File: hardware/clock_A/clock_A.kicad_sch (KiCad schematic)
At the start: 225 parts, among them J1 RJ45, J12 Conn_01x08_Pin, J14 Conn_01x02_Pin, J2 Conn_01x03, J4 USB_C_Receptacle, J5 Conn_01x06_Pin, J6 Conn_01x03_Pin, J8 Conn_01x02_Pin, Q1 2N7002, Q10 2N7002, Q9 2N7002, SW1 SW_Push_4PDT, SW2 SW_SPDT, U1 ADA4807-1, U10 STM32F405RGTx, U11 AMS1117-3.3, U12 BA50DD0WHFP-TR, U13 M24C02-RMN, U14 CH340C, U15 USBLC6-2P6, U16 TLV3603DCKR, U17 SN74LVC1G14DBV, U18 TMP112AIDRLR, U19 SN74LVC1G14DBV, U2 SN74LVC1G14DBV, U20 SN74LVC1G14DBV, U21 SN74LVC1G14DBV, U23 TPS63060, U3 SN74LVC1G14DBV, U4 ADA4807-1, U5 ADA4807-1, U6 TLV3603DCKR, U7 SN74LVC1G14DBV, U8 TLV3603DCKR, U9 L78L05_SOT89, Y1 MultiOsc, Y2 16MHz

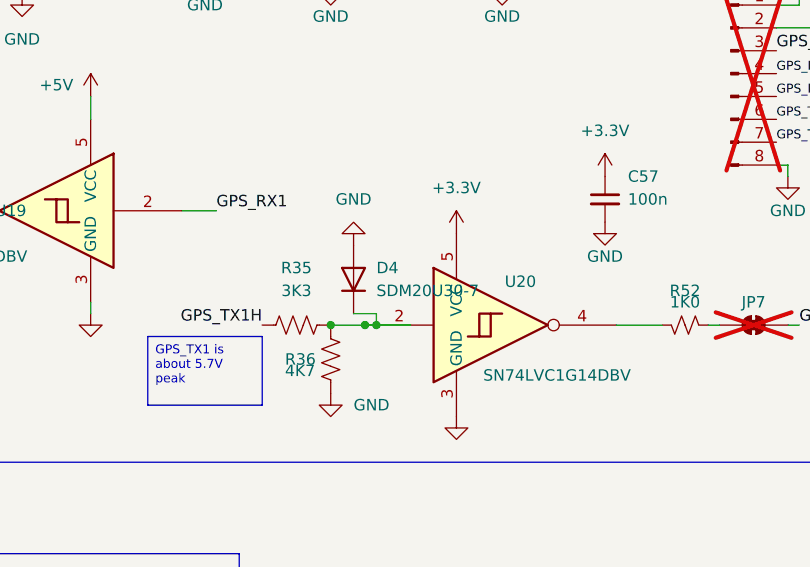
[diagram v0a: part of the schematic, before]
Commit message: updade clock order with correct diode. Fixes #339
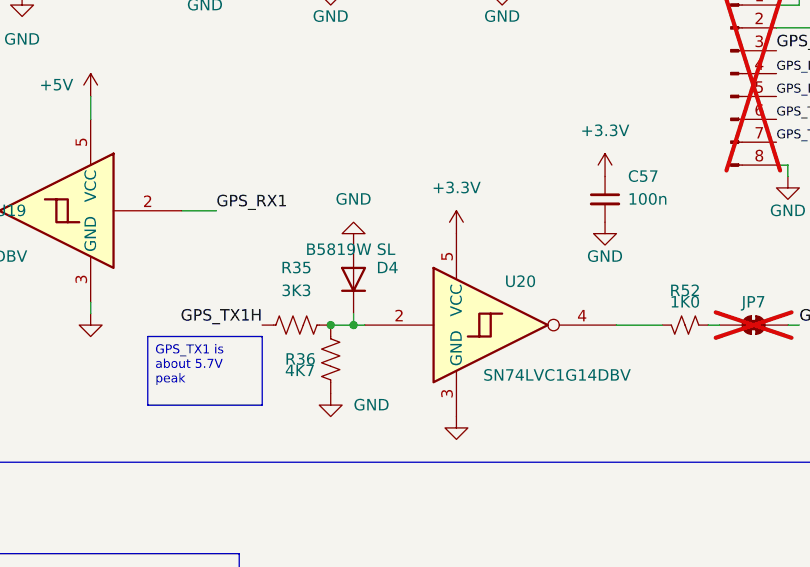
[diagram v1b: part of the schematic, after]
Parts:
- D4: value SDM20U30-7 -> B5819W SL; JLCPCB Part # C91235 -> C8598
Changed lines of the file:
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@@
 	)
 	(junction
-		(at 87.63 300.99)
-		(diameter 0)
-		(color 0 0 0 0)
-	)
-	(junction
 		(at 266.7 278.13)
 		(diameter 0)
@@
 	)
 	(junction
-		(at 83.82 300.99)
-		(diameter 0)
-		(color 0 0 0 0)
-	)
-	(junction
 		(at 123.19 115.57)
 		(diameter 0)
@@
 	)
 	(junction
+		(at 83.82 300.99)
+		(diameter 0)
+		(color 0 0 0 0)
+	)
+	(junction
 		(at 452.12 251.46)
 		(diameter 0)
@@
 	)
 	(junction
+		(at 86.36 300.99)
+		(diameter 0)
+		(color 0 0 0 0)
+	)
+	(junction
 		(at 49.53 72.39)
 		(diameter 0)
@@
 	)
 	(junction
-		(at 88.9 300.99)
-		(diameter 0)
-		(color 0 0 0 0)
-	)
-	(junction
 		(at 373.38 132.08)
 		(diameter 0)
@@
 	(wire
 		(pts
+			(xy 86.36 300.99) (xy 87.63 300.99)
+		)
+		(stroke
+			(width 0)
+			(type default)
+		)
+	)
+	(wire
+		(pts
 			(xy 78.74 80.01) (xy 78.74 81.28)
 		)
@@
 	(wire
 		(pts
-			(xy 83.82 300.99) (xy 87.63 300.99)
-		)
-		(stroke
-			(width 0)
-			(type default)
-		)
-	)
-	(wire
-		(pts
 			(xy 115.57 300.99) (xy 120.65 300.99)
 		)
@@
 	(wire
 		(pts
-			(xy 88.9 300.99) (xy 92.71 300.99)
-		)
-		(stroke
-			(width 0)
-			(type default)
-		)
-	)
-	(wire
-		(pts
 			(xy 298.45 181.61) (xy 298.45 184.15)
 		)
@@
 	(wire
 		(pts
-			(xy 87.63 300.99) (xy 88.9 300.99)
-		)
-		(stroke
-			(width 0)
-			(type default)
-		)
-	)
-	(wire
-		(pts
 			(xy 142.24 49.53) (xy 142.24 53.34)
 		)
@@
 	(wire
 		(pts
-			(xy 88.9 299.72) (xy 88.9 300.99)
-		)
-		(stroke
-			(width 0)
-			(type default)
-		)
-	)
-	(wire
-		(pts
 			(xy 387.35 52.07) (xy 387.35 44.45)
 		)
@@
 	(wire
 		(pts
-			(xy 86.36 299.72) (xy 88.9 299.72)
-		)
-		(stroke
-			(width 0)
-			(type default)
-		)
-	)
-	(wire
-		(pts
 			(xy 52.07 77.47) (xy 52.07 80.01)
 		)
@@
 	(wire
 		(pts
+			(xy 86.36 299.72) (xy 86.36 300.99)
+		)
+		(stroke
+			(width 0)
+			(type default)
+		)
+	)
+	(wire
+		(pts
 			(xy 100.33 125.73) (xy 107.95 125.73)
 		)
@@
 	(wire
 		(pts
+			(xy 83.82 300.99) (xy 86.36 300.99)
+		)
+		(stroke
+			(width 0)
+			(type default)
+		)
+	)
+	(wire
+		(pts
 			(xy 373.38 138.43) (xy 373.38 139.7)
 		)
@@
 		(on_board yes)
 		(dnp no)
-		(fields_autoplaced yes)
 		(property "Reference" "D4"
 			(at 88.9 294.64 90)
@@
 			)
 		)
-		(property "Value" "SDM20U30-7"
-			(at 88.9 297.18 90)
+		(property "Value" "B5819W SL"
+			(at 81.026 292.608 90)
 			(effects
 				(font
@@
 			)
 		)
-		(property "Datasheet" "https://www.vishay.com/docs/85748/1n4148w.pdf"
+		(property "Datasheet" ""
 			(at 86.36 295.91 0)
 			(effects
@@
 			)
 		)
-		(property "Description" "75V 0.15A Fast Switching Diode, SOD-123"
+		(property "Description" "40V 600mV@1A 1A SOD-123 Schottky Barrier Diodes"
 			(at 86.36 295.91 0)
 			(effects
@@
 			)
 		)
-		(property "JLCPCB Part #" "C91235"
+		(property "JLCPCB Part #" "C8598"
 			(at 86.36 295.91 0)
 			(effects

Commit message: update footprints
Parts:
- S1, S3: footprint SW_147873-2 -> blinky_footprints:SW_147873-2
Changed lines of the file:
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@@
 			)
 		)
-		(property "Footprint" "SW_147873-2"
+		(property "Footprint" "blinky_footprints:SW_147873-2"
 			(at 274.32 274.32 0)
 			(effects
@@
 			)
 		)
-		(property "Footprint" "SW_147873-2"
+		(property "Footprint" "blinky_footprints:SW_147873-2"
 			(at 280.67 303.53 0)
 			(effects

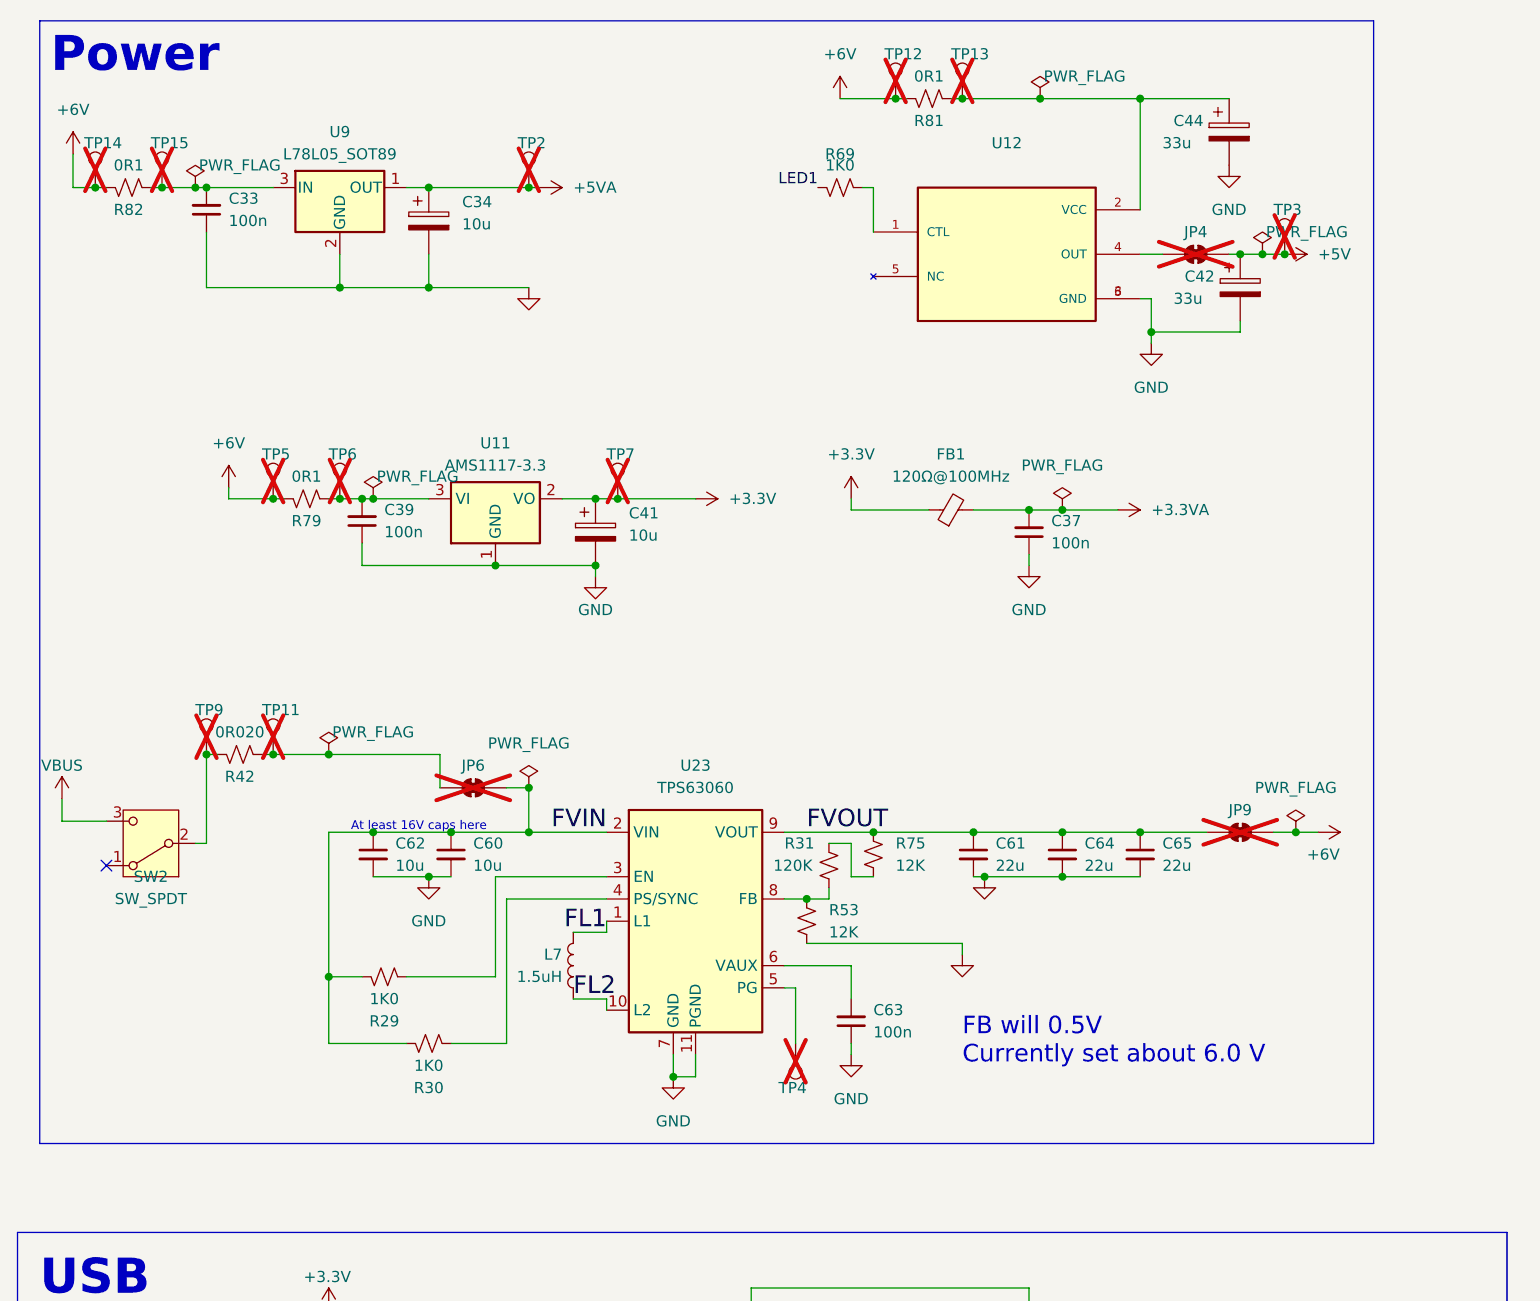
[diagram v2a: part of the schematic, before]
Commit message: remove tantium caps from clock board
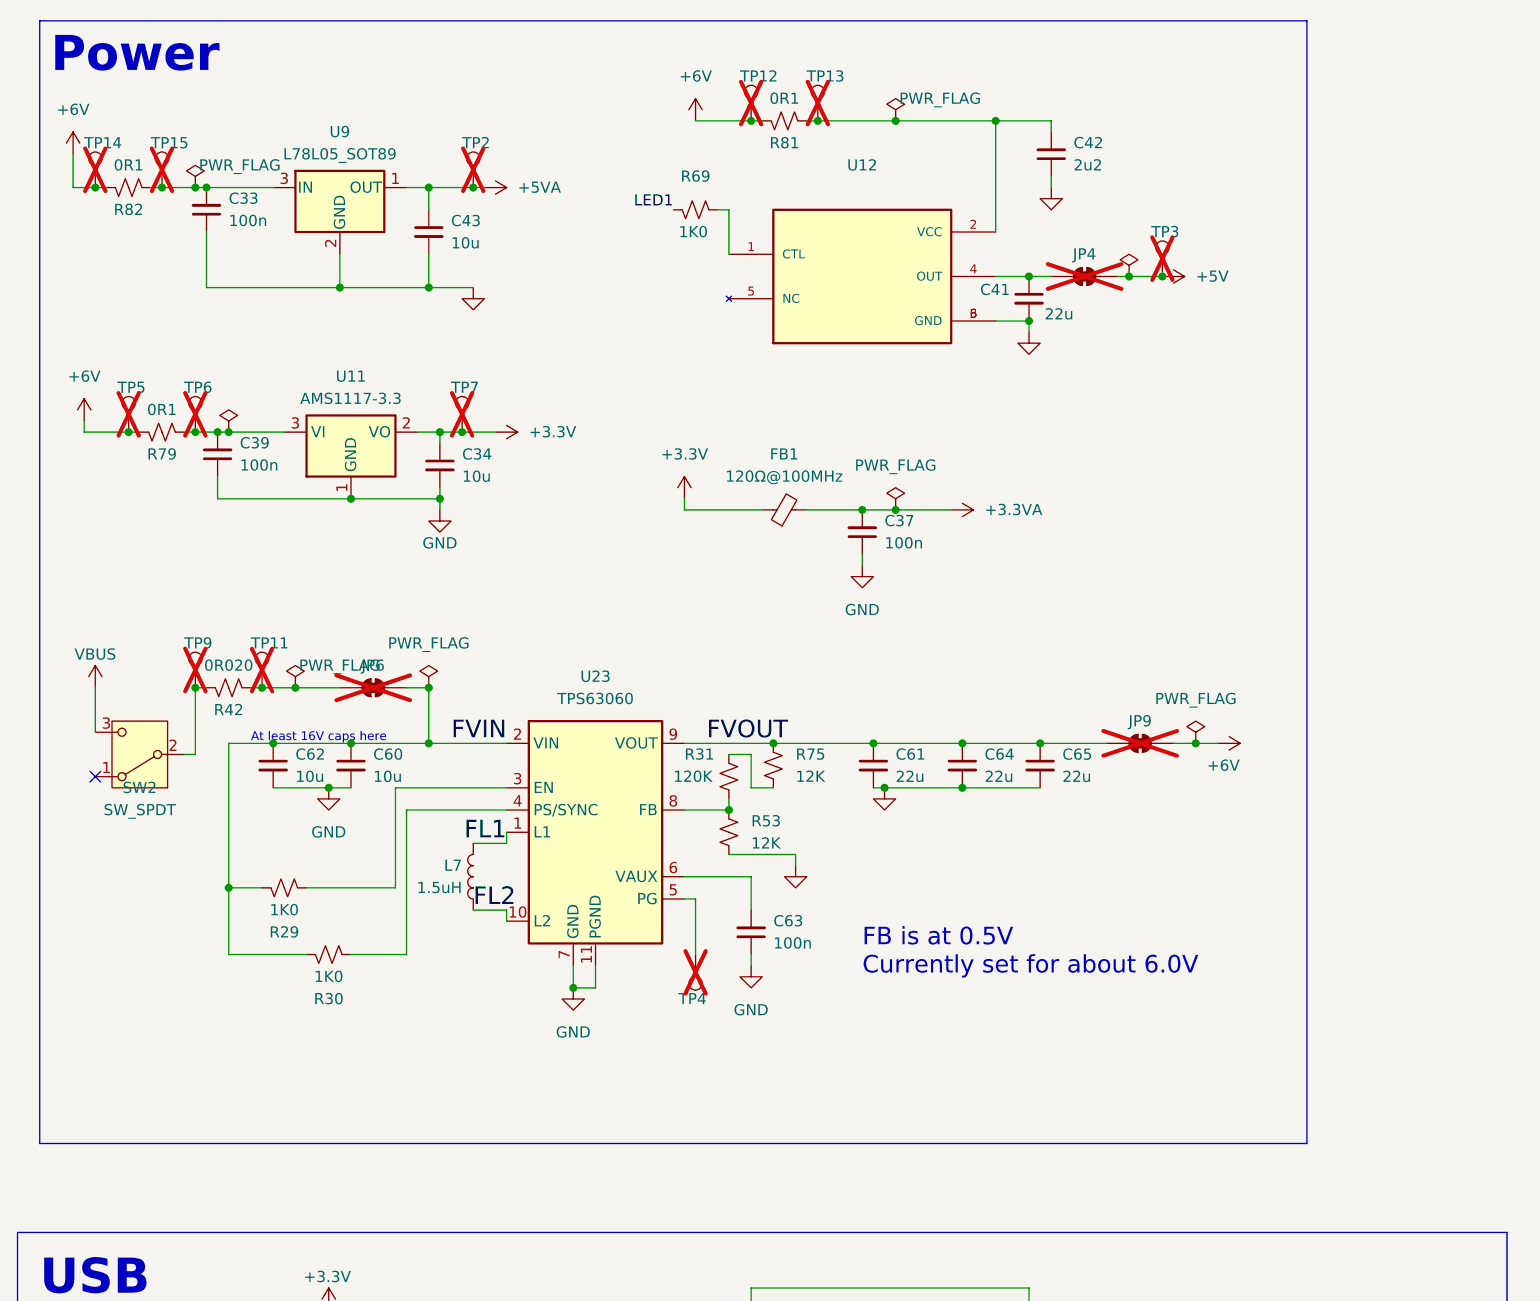
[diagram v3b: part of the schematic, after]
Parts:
- removed C34, C41: 10u, Capacitor_Tantalum_SMD:CP_EIA-3216-18_Kemet-A, symbol Device:C_Polarized
- removed C42, C44: 33u, Capacitor_Tantalum_SMD:CP_EIA-3528-21_Kemet-B, symbol Device:C_Polarized
- added C34, C43: 10u, Capacitor_SMD:C_0603_1608Metric, symbol Device:C_Small
- added C41: 22u, Capacitor_SMD:C_0805_2012Metric, symbol Device:C_Small
- added C42: 2u2, Capacitor_SMD:C_0603_1608Metric, symbol Device:C_Small
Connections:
- net +3.3V: now also C34.1
- net +5VA: now also C43.1
- net GND: now also C34.2, C41.2, C42.1, C43.2
- net at JP4.1 (A), U12.4 (OUT): now also C41.1
- net at R81.1, TP13.1, U12.2 (VCC): now also C42.2
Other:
- note added: "FB is at 0.5V Currently set for about 6.0V"
- note removed: "FB will 0.5V Currently set about 6.0 V"
- moved on the sheet: C37, C39, C60, C61, C62, C63, C64, C65, FB1, JP4, JP6, JP9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

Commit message: update rotation and offsets on clock and gps
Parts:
- D5: JLCPCB Position Offset 0,-0.75 -> 0,0.7
- J2: JLCPCB Position Offset 0,0.0 -> (none); JLCPCB Rotation Offset 180 -> (none)
- J4: JLCPCB Position Offset 0,1.1 -> 0,1.5
- J? (x6): JLCPCB Position Offset (none) -> 0,-13.0
- SW1: JLCPCB Position Offset -1.35,-6.38 -> 0,-6.7
- SW2: JLCPCB Position Offset 3.9,-1.2 -> 0.1,4.1
- TP1, TP10, TP4, TP7, TP8: footprint TestPoint:TestPoint_THTPad_D1.5mm_Drill0.7mm -> TestPoint:TestPoint_THTPad_D1.0mm_Drill0.5mm
- U10, U14: JLCPCB Rotation Offset 270 -> (none)
- U11: JLCPCB Rotation Offset 180 -> (none)
- U16: footprint blinky_footprints:SC70_DCK_TEX -> Package_TO_SOT_SMD:SOT-363_SC-70-6
- U17, U19, U2, U20, U21, U3, U7: JLCPCB Rotation Offset 0 -> (none)
- U18: JLCPCB Rotation Offset 270 -> 180
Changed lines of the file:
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@@
 			)
 		)
+		(property "JLCPCB Position Offset" "0,-13.0"
+			(at 365.76 132.08 0)
+			(effects
+				(font
+					(size 1.27 1.27)
+				)
+				(hide yes)
+			)
+		)
 		(pin "1"
 		)
@@
 			)
 		)
+		(property "JLCPCB Position Offset" "0,-13.0"
+			(at 483.87 214.63 0)
+			(effects
+				(font
+					(size 1.27 1.27)
+				)
+				(hide yes)
+			)
+		)
 		(pin "1"
 		)
@@
 			)
 		)
-		(property "Footprint" "TestPoint:TestPoint_THTPad_D1.5mm_Drill0.7mm"
+		(property "Footprint" "TestPoint:TestPoint_THTPad_D1.0mm_Drill0.5mm"
 			(at 222.25 278.13 0)
 			(effects
@@
 			)
 		)
-		(property "JLCPCB Rotation Offset" "0"
+		(property "JLCPCB Rotation Offset" ""
 			(at 52.07 288.29 0)
 			(effects
@@
 			)
 		)
-		(property "Footprint" "TestPoint:TestPoint_THTPad_D1.5mm_Drill0.7mm"
+		(property "Footprint" "TestPoint:TestPoint_THTPad_D1.0mm_Drill0.5mm"
 			(at 68.58 64.77 0)
 			(effects
@@
 			)
 		)
-		(property "JLCPCB Rotation Offset" "0"
+		(property "JLCPCB Rotation Offset" ""
 			(at 459.74 38.1 0)
 			(effects
@@
 			)
 		)
-		(property "JLCPCB Rotation Offset" "180"
+		(property "JLCPCB Rotation Offset" ""
 			(at 207.01 82.55 0)
 			(effects
@@
 			)
 		)
-		(property "JLCPCB Position Offset" "0,0.0"
+		(property "JLCPCB Position Offset" ""
 			(at 207.01 82.55 0)
 			(effects
@@
 			)
 		)
-		(property "JLCPCB Rotation Offset" "270"
+		(property "JLCPCB Rotation Offset" ""
 			(at 267.97 83.82 0)
 			(effects
@@
 			)
 		)
-		(property "JLCPCB Position Offset" "0,1.1"
+		(property "JLCPCB Position Offset" "0,1.5"
 			(at 135.89 194.31 0)
 			(effects
@@
 			)
 		)
-		(property "Footprint" "TestPoint:TestPoint_THTPad_D1.5mm_Drill0.7mm"
+		(property "Footprint" "TestPoint:TestPoint_THTPad_D1.0mm_Drill0.5mm"
 			(at 453.39 86.36 0)
 			(effects
@@
 			)
 		)
+		(property "JLCPCB Position Offset" "0,-13.0"
+			(at 480.06 180.34 0)
+			(effects
+				(font
+					(size 1.27 1.27)
+				)
+				(hide yes)
+			)
+		)
 		(pin "1"
 		)
@@
 			)
 		)
-		(property "JLCPCB Rotation Offset" "270"
+		(property "JLCPCB Rotation Offset" "180"
 			(at 236.22 229.87 0)
 			(effects
@@
 			)
 		)
-		(property "JLCPCB Rotation Offset" "180"
+		(property "JLCPCB Rotation Offset" ""
 			(at 50.8 64.77 0)
 			(effects
@@
 			)
 		)
-		(property "JLCPCB Rotation Offset" "0"
+		(property "JLCPCB Rotation Offset" ""
 			(at 476.25 132.08 0)
 			(effects
@@
 			)
 		)
-		(property "JLCPCB Rotation Offset" "0"
+		(property "JLCPCB Rotation Offset" ""
 			(at 430.53 86.36 0)
 			(effects
@@
 			)
 		)
-		(property "JLCPCB Position Offset" "3.9,-1.2"
+		(property "JLCPCB Position Offset" "0.1,4.1"
 			(at 26.67 101.6 0)
 			(effects
@@
 			)
 		)
-		(property "JLCPCB Rotation Offset" "0"
+		(property "JLCPCB Rotation Offset" ""
 			(at 396.24 132.08 0)
 			(effects
@@
 			)
 		)
-		(property "Footprint" "blinky_footprints:SC70_DCK_TEX"
+		(property "Footprint" "Package_TO_SOT_SMD:SOT-363_SC-70-6"
 			(at 421.64 38.1 0)
 			(effects
@@
 			)
 		)
-		(property "JLCPCB Rotation Offset" "270"
+		(property "JLCPCB Rotation Offset" ""
 			(at 45.72 191.77 0)
 			(effects
@@
 			)
 		)
-		(property "JLCPCB Rotation Offset" "0"
+		(property "JLCPCB Rotation Offset" ""
 			(at 102.87 300.99 0)
 			(effects
@@
 			)
 		)
-		(property "Footprint" "TestPoint:TestPoint_THTPad_D1.5mm_Drill0.7mm"
+		(property "Footprint" "TestPoint:TestPoint_THTPad_D1.0mm_Drill0.5mm"
 			(at 483.87 38.1 0)
 			(effects
@@
 			)
 		)
-		(property "Footprint" "TestPoint:TestPoint_THTPad_D1.5mm_Drill0.7mm"
+		(property "Footprint" "TestPoint:TestPoint_THTPad_D1.0mm_Drill0.5mm"
 			(at 85.09 124.46 0)
 			(effects
@@
 			)
 		)
-		(property "JLCPCB Rotation Offset" "0"
+		(property "JLCPCB Rotation Offset" ""
 			(at 229.87 278.13 0)
 			(effects
@@
 			)
 		)
-		(property "JLCPCB Position Offset" "-1.35,-6.38"
+		(property "JLCPCB Position Offset" "0,-6.7"
 			(at 237.49 358.14 0)
 			(effects
@@
 			)
 		)
+		(property "JLCPCB Position Offset" "0,-13.0"
+			(at 511.81 132.08 0)
+			(effects
+				(font
+					(size 1.27 1.27)
+				)
+				(hide yes)
+			)
+		)
 		(pin "1"
 		)
@@
 			)
 		)
+		(property "JLCPCB Position Offset" "0,-13.0"
+			(at 480.06 248.92 0)
+			(effects
+				(font
+					(size 1.27 1.27)
+				)
+				(hide yes)
+			)
+		)
 		(pin "1"
 		)
@@
 			)
 		)
-		(property "JLCPCB Position Offset" "0,-0.75"
+		(property "JLCPCB Position Offset" "0,0.7"
 			(at 295.91 334.01 0)
 			(effects
@@
 			(at 361.95 44.45 0)
 			(effects
+				(font
+					(size 1.27 1.27)
+				)
+				(hide yes)
+			)
+		)
+		(property "JLCPCB Position Offset" "0,-13.0"
+			(at 361.95 44.45 0)
+			(effects

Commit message: Update jlc part num for CH340 Fixes#346
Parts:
- U14: JLCPCB Part # C84681 -> C7464026
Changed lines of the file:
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@@
 			)
 		)
-		(property "JLCPCB Part #" "C84681"
+		(property "JLCPCB Part #" "C7464026"
 			(at 45.72 191.77 0)
 			(effects

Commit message: updates for Clock Rev A.2
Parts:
- Q1, Q10, Q9: JLCPCB Rotation Offset 180 -> (none)
- U1, U4, U5: JLCPCB Rotation Offset 270 -> 90
- U13: JLCPCB Rotation Offset 270 -> (none)
- U9: JLCPCB Position Offset 0.5,0 -> -0.75,0; JLCPCB Rotation Offset 180 -> (none)
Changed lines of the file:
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@@
 			)
 		)
-		(property "JLCPCB Rotation Offset" "180"
+		(property "JLCPCB Rotation Offset" ""
 			(at 270.51 341.63 0)
 			(effects
@@
 			)
 		)
-		(property "JLCPCB Rotation Offset" "270"
+		(property "JLCPCB Rotation Offset" "90"
 			(at 405.13 214.63 0)
 			(effects
@@
 			)
 		)
-		(property "JLCPCB Rotation Offset" "180"
+		(property "JLCPCB Rotation Offset" ""
 			(at 270.51 364.49 0)
 			(effects
@@
 			)
 		)
-		(property "JLCPCB Rotation Offset" "180"
+		(property "JLCPCB Rotation Offset" ""
 			(at 49.53 36.83 0)
 			(effects
@@
 			)
 		)
-		(property "JLCPCB Position Offset" "0.5,0"
+		(property "JLCPCB Position Offset" "-0.75,0"
 			(at 49.53 36.83 0)
 			(effects
@@
 			)
 		)
-		(property "JLCPCB Rotation Offset" "180"
+		(property "JLCPCB Rotation Offset" ""
 			(at 270.51 384.81 0)
 			(effects
@@
 			)
 		)
-		(property "JLCPCB Rotation Offset" "270"
+		(property "JLCPCB Rotation Offset" "90"
 			(at 401.32 248.92 0)
 			(effects
@@
 			)
 		)
-		(property "JLCPCB Rotation Offset" "270"
+		(property "JLCPCB Rotation Offset" ""
 			(at 281.94 228.6 0)
 			(effects
@@
 			)
 		)
-		(property "JLCPCB Rotation Offset" "270"
+		(property "JLCPCB Rotation Offset" "90"
 			(at 401.32 180.34 0)
 			(effects

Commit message: update all harware revs
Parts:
- added R40: 1K0, Resistor_SMD:R_0603_1608Metric, symbol Device:R_Small_US
- FB1: value 120Ω@100MHz -> 120Ω@100MHz
- Y2: value 16MHz -> 16MHz
- gave numbers to parts that had none: 7
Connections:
- net USB_DTR: now also R40.1; no longer J8.1 (Pin_1), JP1.1 (A)
- new net: J8.1 (Pin_1), JP1.1 (A), R40.2
